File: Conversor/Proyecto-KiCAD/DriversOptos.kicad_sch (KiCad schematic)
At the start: 27 parts, among them U10 ACPL-P480, U11 ACPL-P480, U12 2ED21834-S06J, U13 2ED21834-S06J, U8 ACPL-P480, U9 ACPL-P480

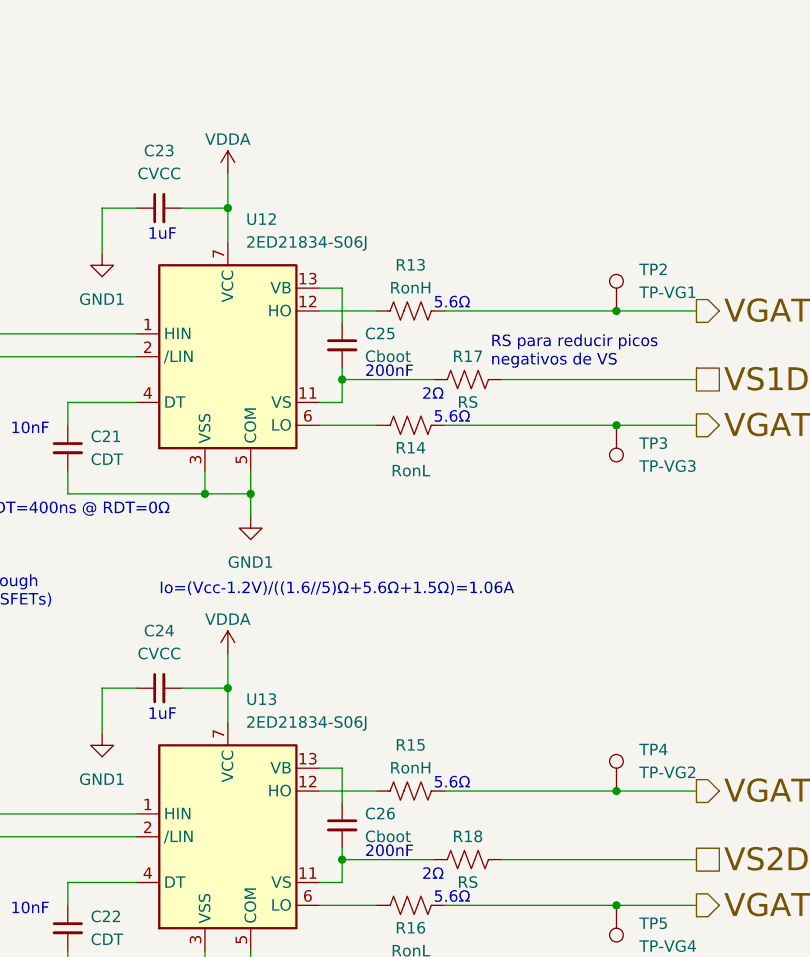
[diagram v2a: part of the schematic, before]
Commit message: Empezar con lar recomendaciones de Jorge
- Agregar nota que contiene todas las recomendaciones (ticks en las que
ya hice)
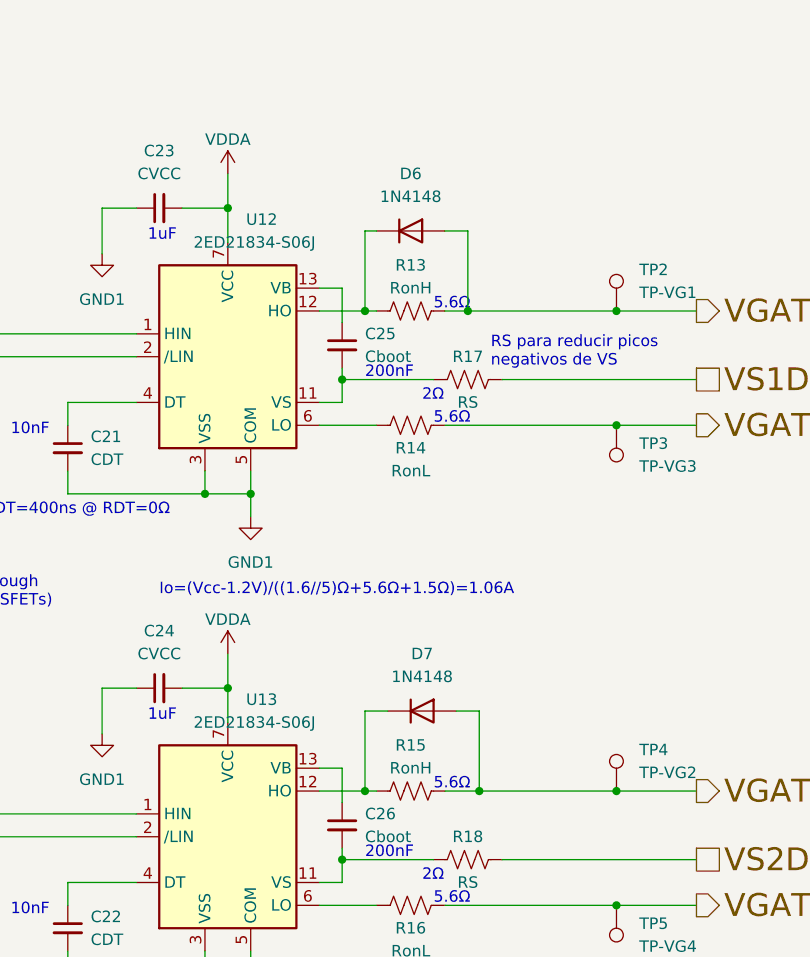
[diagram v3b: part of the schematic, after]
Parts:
- added D6, D7: 1N4148, Diode_THT:D_DO-35_SOD27_P7.62mm_Horizontal, symbol Diode:1N4148
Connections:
- net VGATE1: now also D6.2 (A)
- net VGATE2: now also D7.2 (A)
- net at R15.1, U13.12 (HO): now also D7.1 (K)
- net at R13.1, U12.12 (HO): now also D6.1 (K)
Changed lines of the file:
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@@
 (kicad_sch (version 20211123) (generator eeschema)
   (paper "A4")
+  (junction (at 219.71 116.84) (diameter 0) (color 0 0 0 0)
+  )
   (junction (at 234.95 129.54) (diameter 0) (color 0 0 0 0)
   )
@@
   (junction (at 194.31 83.82) (diameter 0) (color 0 0 0 0)
   )
+  (junction (at 218.44 63.5) (diameter 0) (color 0 0 0 0)
+  )
   (junction (at 144.78 46.99) (diameter 0) (color 0 0 0 0)
   )
@@
   (junction (at 144.78 67.31) (diameter 0) (color 0 0 0 0)
   )
+  (junction (at 207.01 63.5) (diameter 0) (color 0 0 0 0)
+  )
   (junction (at 234.95 116.84) (diameter 0) (color 0 0 0 0)
   )
   (junction (at 144.78 106.68) (diameter 0) (color 0 0 0 0)
   )
+  (junction (at 207.01 116.84) (diameter 0) (color 0 0 0 0)
+  )
   (junction (at 189.23 83.82) (diameter 0) (color 0 0 0 0)
   )
@@
     (stroke (width 0) (type default) (color 0 0 0 0))
   )
-  (wire (pts (xy 215.9 116.84) (xy 234.95 116.84))
+  (wire (pts (xy 215.9 116.84) (xy 219.71 116.84))
     (stroke (width 0) (type default) (color 0 0 0 0))
   )
@@
     (stroke (width 0) (type default) (color 0 0 0 0))
   )
+  (wire (pts (xy 207.01 116.84) (xy 208.28 116.84))
+    (stroke (width 0) (type default) (color 0 0 0 0))
+  )
   (wire (pts (xy 144.78 127) (xy 147.32 127))
     (stroke (width 0) (type default) (color 0 0 0 0))
@@
     (stroke (width 0) (type default) (color 0 0 0 0))
   )
+  (wire (pts (xy 219.71 116.84) (xy 234.95 116.84))
+    (stroke (width 0) (type default) (color 0 0 0 0))
+  )
   (wire (pts (xy 91.44 62.23) (xy 91.44 71.12))
     (stroke (width 0) (type default) (color 0 0 0 0))
@@
     (stroke (width 0) (type default) (color 0 0 0 0))
   )
+  (wire (pts (xy 218.44 54.61) (xy 218.44 63.5))
+    (stroke (width 0) (type default) (color 0 0 0 0))
+  )
   (wire (pts (xy 152.4 106.68) (xy 156.21 106.68))
     (stroke (width 0) (type default) (color 0 0 0 0))
   )
+  (wire (pts (xy 209.55 107.95) (xy 207.01 107.95))
+    (stroke (width 0) (type default) (color 0 0 0 0))
+  )
   (wire (pts (xy 60.96 86.36) (xy 60.96 59.69))
     (stroke (width 0) (type default) (color 0 0 0 0))
@@
     (stroke (width 0) (type default) (color 0 0 0 0))
   )
-  (wire (pts (xy 201.93 116.84) (xy 208.28 116.84))
+  (wire (pts (xy 201.93 116.84) (xy 207.01 116.84))
     (stroke (width 0) (type default) (color 0 0 0 0))
   )
@@
     (stroke (width 0) (type default) (color 0 0 0 0))
   )
+  (wire (pts (xy 207.01 63.5) (xy 208.28 63.5))
+    (stroke (width 0) (type default) (color 0 0 0 0))
+  )
   (wire (pts (xy 138.43 118.11) (xy 138.43 119.38))
     (stroke (width 0) (type default) (color 0 0 0 0))
@@
     (stroke (width 0) (type default) (color 0 0 0 0))
   )
+  (wire (pts (xy 208.28 54.61) (xy 207.01 54.61))
+    (stroke (width 0) (type default) (color 0 0 0 0))
+  )
   (wire (pts (xy 181.61 52.07) (xy 177.8 52.07))
     (stroke (width 0) (type default) (color 0 0 0 0))
@@
     (stroke (width 0) (type default) (color 0 0 0 0))
   )
-  (wire (pts (xy 201.93 63.5) (xy 208.28 63.5))
+  (wire (pts (xy 201.93 63.5) (xy 207.01 63.5))
     (stroke (width 0) (type default) (color 0 0 0 0))
   )
@@
     (stroke (width 0) (type default) (color 0 0 0 0))
   )
+  (wire (pts (xy 218.44 63.5) (xy 234.95 63.5))
+    (stroke (width 0) (type default) (color 0 0 0 0))
+  )
   (wire (pts (xy 137.16 110.49) (xy 144.78 110.49))
     (stroke (width 0) (type default) (color 0 0 0 0))
   )
+  (wire (pts (xy 207.01 107.95) (xy 207.01 116.84))
+    (stroke (width 0) (type default) (color 0 0 0 0))
+  )
   (wire (pts (xy 204.47 64.77) (xy 204.47 60.96))
     (stroke (width 0) (type default) (color 0 0 0 0))
@@
     (stroke (width 0) (type default) (color 0 0 0 0))
   )
+  (wire (pts (xy 219.71 107.95) (xy 219.71 116.84))
+    (stroke (width 0) (type default) (color 0 0 0 0))
+  )
   (wire (pts (xy 162.56 54.61) (xy 162.56 66.04))
     (stroke (width 0) (type default) (color 0 0 0 0))
@@
     (stroke (width 0) (type default) (color 0 0 0 0))
   )
+  (wire (pts (xy 217.17 107.95) (xy 219.71 107.95))
+    (stroke (width 0) (type default) (color 0 0 0 0))
+  )
+  (wire (pts (xy 207.01 54.61) (xy 207.01 63.5))
+    (stroke (width 0) (type default) (color 0 0 0 0))
+  )
   (wire (pts (xy 201.93 127) (xy 204.47 127))
     (stroke (width 0) (type default) (color 0 0 0 0))
   )
   (wire (pts (xy 173.99 83.82) (xy 189.23 83.82))
+    (stroke (width 0) (type default) (color 0 0 0 0))
+  )
+  (wire (pts (xy 215.9 54.61) (xy 218.44 54.61))
     (stroke (width 0) (type default) (color 0 0 0 0))
   )
@@
     (stroke (width 0) (type default) (color 0 0 0 0))
   )
-  (wire (pts (xy 215.9 63.5) (xy 234.95 63.5))
+  (wire (pts (xy 215.9 63.5) (xy 218.44 63.5))
     (stroke (width 0) (type default) (color 0 0 0 0))
   )
@@
   )
   (symbol (lib_id "Componentes proyecto:2ED21834-S06J") (at 191.77 121.92 0) (unit 1)
-    (in_bom yes) (on_board yes) (fields_autoplaced)
+    (in_bom yes) (on_board yes)
     (property "Reference" "U13" (id 0) (at 193.7894 106.68 0)
       (effects (font (size 1.27 1.27)) (justify left))
     )
-    (property "Value" "2ED21834-S06J" (id 1) (at 193.7894 109.22 0)
+    (property "Value" "2ED21834-S06J" (id 1) (at 187.96 109.22 0)
       (effects (font (size 1.27 1.27)) (justify left))
     )
@@
     (pin "9")
   )
+  (symbol (lib_id "Diode:1N4148") (at 212.09 54.61 0) (unit 1)
+    (in_bom yes) (on_board yes) (fields_autoplaced)
+    (property "Reference" "D6" (id 0) (at 212.09 48.26 0))
+    (property "Value" "1N4148" (id 1) (at 212.09 50.8 0))
+    (property "Footprint" "Diode_THT:D_DO-35_SOD27_P7.62mm_Horizontal" (id 2) (at 212.09 59.055 0)
+      (effects (font (size 1.27 1.27)) hide)
+    )
+    (property "Datasheet" "https://assets.nexperia.com/documents/data-sheet/1N4148_1N4448.pdf" (id 3) (at 212.09 54.61 0)
+      (effects (font (size 1.27 1.27)) hide)
+    )
+    (pin "1")
+    (pin "2")
+  )
   (symbol (lib_id "power:GND1") (at 154.94 127 0) (unit 1)
     (in_bom yes) (on_board yes) (fields_autoplaced)
@@
     (pin "1")
   )
+  (symbol (lib_id "Diode:1N4148") (at 213.36 107.95 0) (unit 1)
+    (in_bom yes) (on_board yes) (fields_autoplaced)
+    (property "Reference" "D7" (id 0) (at 213.36 101.6 0))
+    (property "Value" "1N4148" (id 1) (at 213.36 104.14 0))
+    (property "Footprint" "Diode_THT:D_DO-35_SOD27_P7.62mm_Horizontal" (id 2) (at 213.36 112.395 0)
+      (effects (font (size 1.27 1.27)) hide)
+    )
+    (property "Datasheet" "https://assets.nexperia.com/documents/data-sheet/1N4148_1N4448.pdf" (id 3) (at 213.36 107.95 0)
+      (effects (font (size 1.27 1.27)) hide)
+    )
+    (pin "1")
+    (pin "2")
+  )
   (symbol (lib_id "Device:C_Small") (at 149.86 46.99 90) (unit 1)
     (in_bom yes) (on_board yes)
@@
   )
   (symbol (lib_name "2ED21834-S06J_1") (lib_id "Componentes proyecto:2ED21834-S06J") (at 191.77 68.58 0) (unit 1)
-    (in_bom yes) (on_board yes) (fields_autoplaced)
+    (in_bom yes) (on_board yes)
     (property "Reference" "U12" (id 0) (at 193.7894 53.34 0)
       (effects (font (size 1.27 1.27)) (justify left))
     )
-    (property "Value" "2ED21834-S06J" (id 1) (at 193.7894 55.88 0)
-      (effects (font (size 1.27 1.27)) (justify left))
-    )
+    (property "Value" "2ED21834-S06J" (id 1) (at 187.96 55.88 0)
+      (effects (font (size 1.27 1.27)) (justify left))
+    )
